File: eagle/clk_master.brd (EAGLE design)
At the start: 76.2 x 50.8 mm, 68 parts, among them U1 74LVCU04A, U2 MCP1824ST-3302E, U3 ATXMEGA16A4U, U4 ENC28J60, U5 TESEO-LIV3R, U8 74LVC74A, U9 74LVC86A

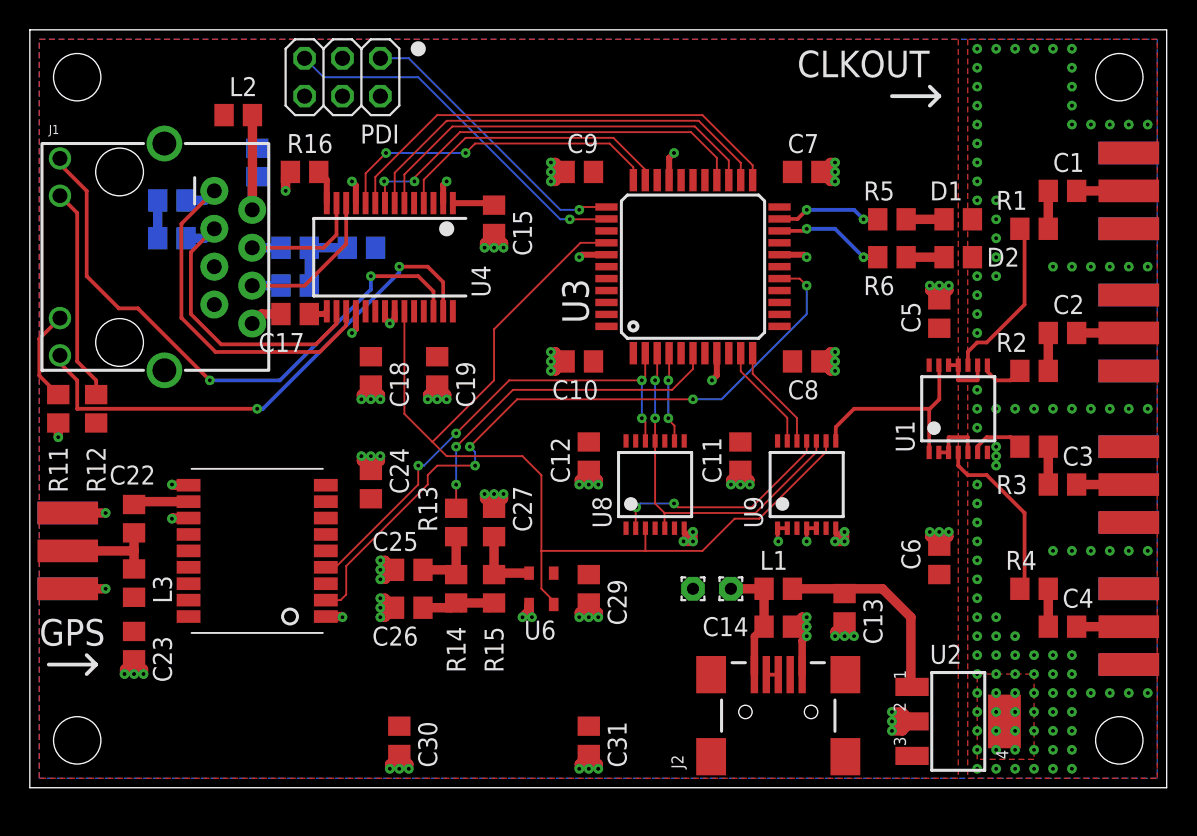
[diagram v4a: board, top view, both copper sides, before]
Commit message: fix en28j60 spi
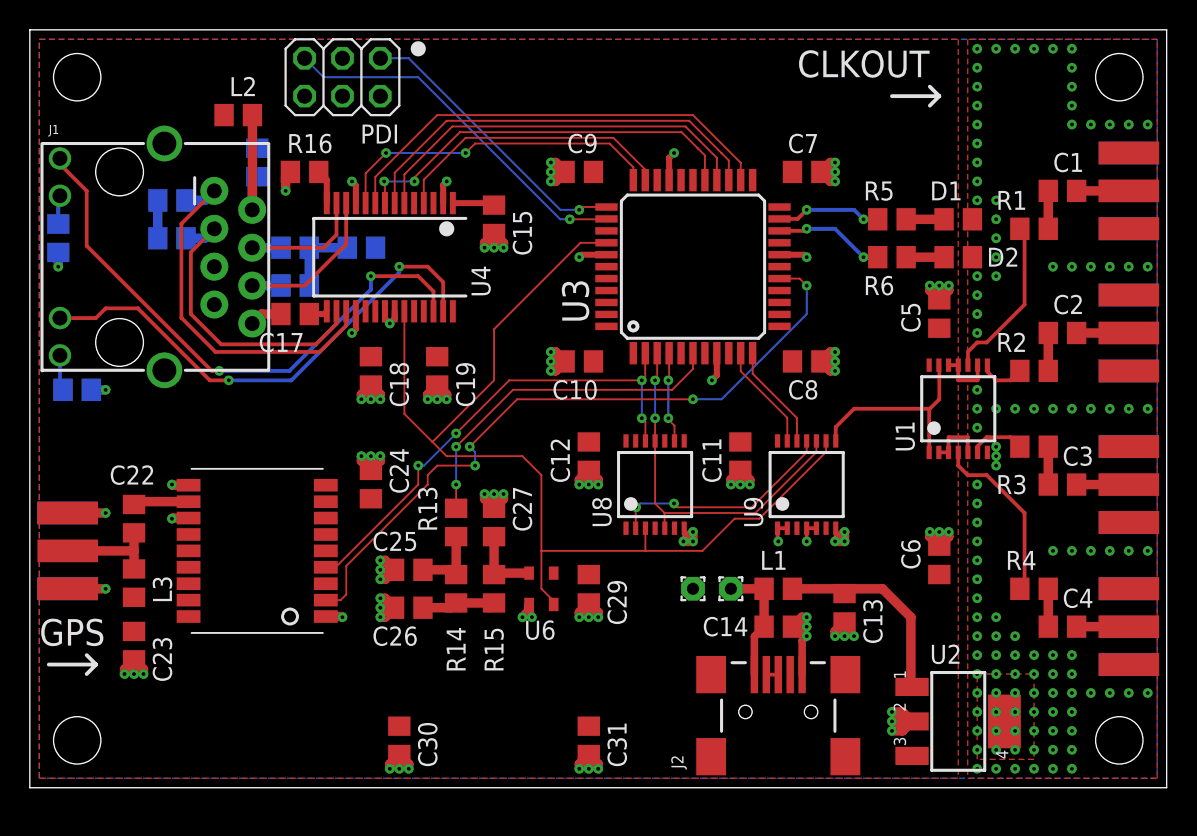
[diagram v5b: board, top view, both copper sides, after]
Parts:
- moved R12 11.7 mm to (1.91, 36.8), flipped to the bottom
- moved R11 1.80 mm to (3.17, 26.7), flipped to the bottom, turned to 180 degrees
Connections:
- net S$1 renamed OUT0
- net S$15 renamed BPSK
- net S$16 renamed FILT1
- net S$17 renamed FILT0
- net S$18 renamed FILT
- net S$2 renamed OUT1
- net S$23 renamed CLK_25MHZ
- net S$24 renamed SPPS
- net S$25 renamed DAC0
- net S$26 renamed UPPS
- net S$27 renamed CCA
- net S$28 renamed CCB
- net S$29 renamed U/!D
- net S$3 renamed OUT2
- net S$34 renamed !RST
- net S$35 renamed !INT
- net S$38 renamed LED0
- net S$39 renamed LED1
- net S$4 renamed OUT3
- net S$40 renamed GPS_ANT
- net S$41 renamed GPS_ANT1
- net S$42 renamed GPS_TX
- net S$43 renamed PDI
- net S$44 renamed !RESET
- net S$55 renamed LEDB
- removed net S$30: U3.23, U4.9
- removed net S$31: U3.24, U4.7
- removed net S$32: U3.25, U4.6
- removed net S$33: U3.26, U4.8
- removed net S$52: J1.11, R11.1
- removed net S$56: J1.12, U4.27
- new net !SS: U3.24, U4.9
- new net LEDA: J1.11, U4.27
- new net MISO: U3.26, U4.6
- new net MOSI: U3.25, U4.7
- new net S$19: J1.12, R11.1
- new net SCK: U3.27, U4.8
- net GND: no longer R11.2
- net V3.3: now also R11.2
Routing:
- net S$56: track 35.1 -> 0.00 mm, vias 2 -> 0
- net LEDA: track 0.00 -> 33.7 mm, vias 0 -> 2
- net S$30: track 31.2 -> 0.00 mm
- net !SS: track 0.00 -> 30.4 mm
- net S$31: track 29.0 -> 0.00 mm
- net MOSI: track 0.00 -> 28.3 mm
- net S$33: track 27.5 -> 0.00 mm, vias 2 -> 0
- net S$32: track 27.3 -> 0.00 mm
- net SCK: track 0.00 -> 26.8 mm, vias 0 -> 2
- net MISO: track 0.00 -> 26.6 mm
- net S$54: track 14.3 -> 1.95 mm
- net S$52: track 6.23 -> 0.00 mm
- net S$19: track 0.00 -> 2.39 mm
- net V3.3: track 1.25 -> 3.16 mm, vias 0 -> 2
- net LEDB: track 39.9 -> 38.2 mm
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
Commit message: name more signals on board layout
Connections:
- net S$45 renamed TPIN+
- net S$46 renamed TPIN-
- net S$47 renamed TPOUT+
- net S$48 renamed TPOUT-
- net S$53 renamed RBIAS
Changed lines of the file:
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@@
 <wire x1="38.625" y1="38.1" x2="38.65" y2="38.125" width="0.127" layer="1"/>
 </signal>
-<signal name="S$45">
+<signal name="TPIN+">
 <contactref element="U4" pad="13"/>
 <contactref element="J1" pad="4"/>
@@
 <wire x1="19.685" y1="36.195" x2="14.905" y2="36.195" width="0.254" layer="1"/>
 </signal>
-<signal name="S$46">
+<signal name="TPIN-">
 <contactref element="U4" pad="12"/>
 <contactref element="J1" pad="6"/>
@@
 <wire x1="18.415" y1="33.655" x2="14.905" y2="33.655" width="0.254" layer="1"/>
 </signal>
-<signal name="S$47">
+<signal name="TPOUT+">
 <contactref element="J1" pad="1"/>
 <contactref element="R9" pad="1"/>
@@
 <wire x1="21.205" y1="30.984" x2="19.431" y2="29.21" width="0.254" layer="1"/>
 </signal>
-<signal name="S$48">
+<signal name="TPOUT-">
 <contactref element="J1" pad="3"/>
 <contactref element="R10" pad="1"/>
@@
 <wire x1="14.92" y1="38.75" x2="14.905" y2="38.735" width="0.635" layer="1"/>
 </signal>
-<signal name="S$53">
+<signal name="RBIAS">
 <contactref element="U4" pad="14"/>
 <contactref element="R16" pad="1"/>
